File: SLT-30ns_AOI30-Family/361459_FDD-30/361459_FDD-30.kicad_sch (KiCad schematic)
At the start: 9 parts, among them U1 12-Pin_SLx_Can

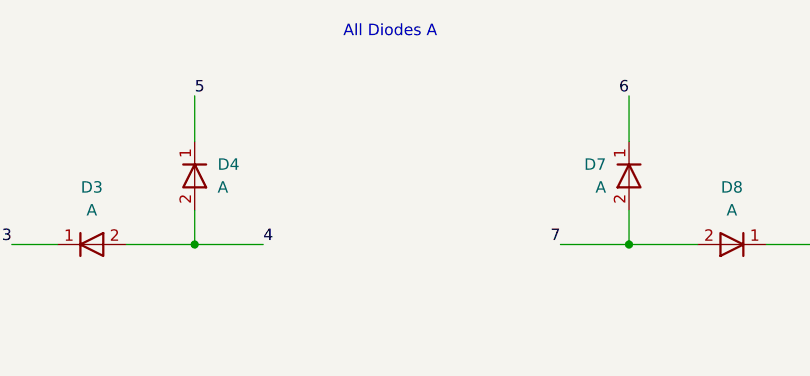
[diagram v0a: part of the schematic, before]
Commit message: Update schematic pdfs
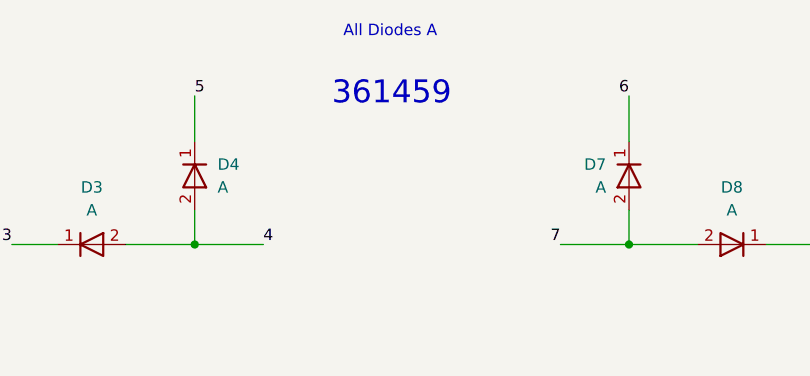
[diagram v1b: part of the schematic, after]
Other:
- note added: "361459"
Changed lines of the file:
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@@
     (effects (font (size 1.27 1.27)) (justify left bottom))
+  )
+  (text "361459" (at 111.76 64.77 0)
+    (effects (font (size 2.54 2.54)) (justify left bottom))
   )
   (label "9" (at 248.92 137.16 0)
